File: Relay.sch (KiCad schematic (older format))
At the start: 11 parts, among them K1 1461069-5, Q1 2N3404, U1 LTV-816S

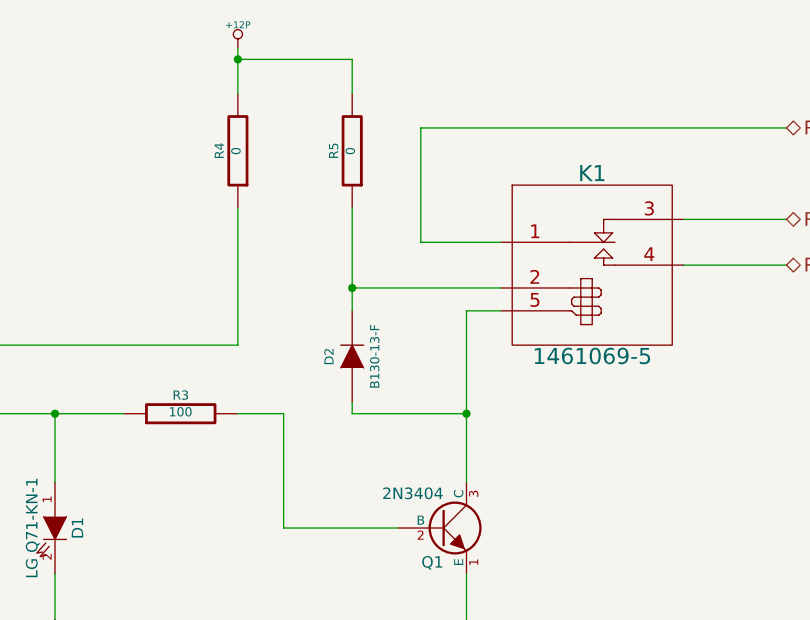
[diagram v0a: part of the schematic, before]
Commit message: Test points added, silk screen updates
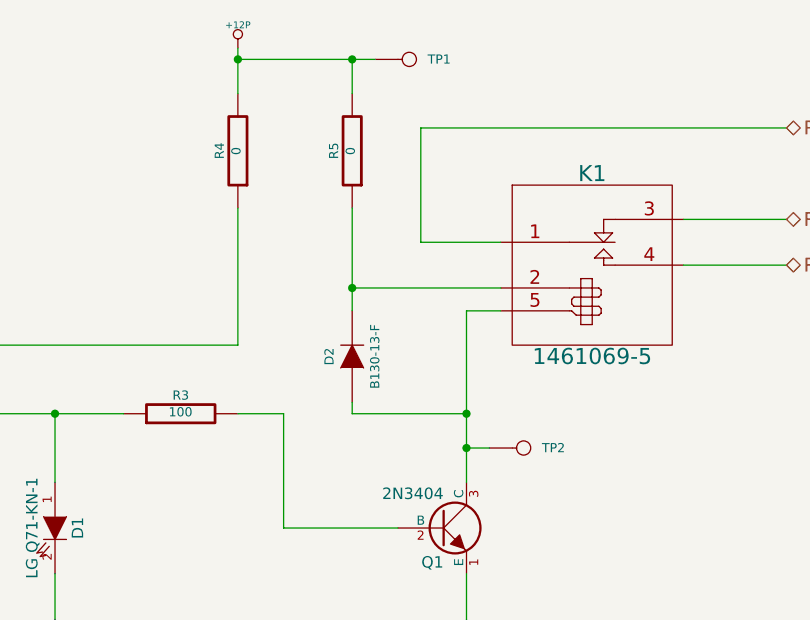
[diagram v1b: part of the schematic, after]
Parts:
- added TP1: +12P, symbol CONN_1
- added TP2: RLY_LOW, symbol CONN_1
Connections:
- net +12P: now also TP1.1
- net at D2.1 (A), K1.5 (COIL-), Q1.3 (C): now also TP2.1
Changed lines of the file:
@@
 	6100 3100 5900 3100
 $Comp
-L +12P #PWR1
+L +12P #PWR01
 U 1 1 52F17C6A
 P 5900 1500
-F 0 "#PWR1" H 5900 1470 30  0001 C CNN
+F 0 "#PWR01" H 5900 1470 30  0001 C CNN
 F 1 "+12P" H 5900 1600 30  0000 C CNN
 F 2 "" H 5900 1500 60  0000 C CNN
@@
 	6400 1700 6400 1550
 Wire Wire Line
-	6400 1550 5900 1550
+	5900 1550 6500 1550
 Connection ~ 5900 1550
 Wire Wire Line
@@
 Connection ~ 6400 2550
 $Comp
-L GND_RELAY #PWR2
+L GND_RELAY #PWR02
 U 1 1 53152624
 P 6900 4800
-F 0 "#PWR2" H 6900 4800 30  0001 C CNN
+F 0 "#PWR02" H 6900 4800 30  0001 C CNN
 F 1 "GND_RELAY" H 6900 4730 30  0000 C CNN
 F 2 "" H 6900 4800 60  0000 C CNN
@@
 	1    0    0    -1
 $EndComp
+$Comp
+L CONN_1 TP2
+U 1 1 532249E8
+P 7150 3250
+F 0 "TP2" H 7230 3250 40  0000 L CNN
+F 1 "RLY_LOW" H 7150 3305 30  0001 C CNN
+F 2 "" H 7150 3250 60  0000 C CNN
+F 3 "" H 7150 3250 60  0000 C CNN
+	1    7150 3250
+	1    0    0    -1
+$EndComp
+Wire Wire Line
+	7000 3250 6900 3250
+Connection ~ 6900 3250
+$Comp
+L CONN_1 TP1
+U 1 1 53224A4C
+P 6650 1550
+F 0 "TP1" H 6730 1550 40  0000 L CNN
+F 1 "+12P" H 6650 1605 30  0001 C CNN
+F 2 "" H 6650 1550 60  0000 C CNN
+F 3 "" H 6650 1550 60  0000 C CNN
+	1    6650 1550
+	1    0    0    -1
+$EndComp
+Connection ~ 6400 1550
 $EndSCHEMATC

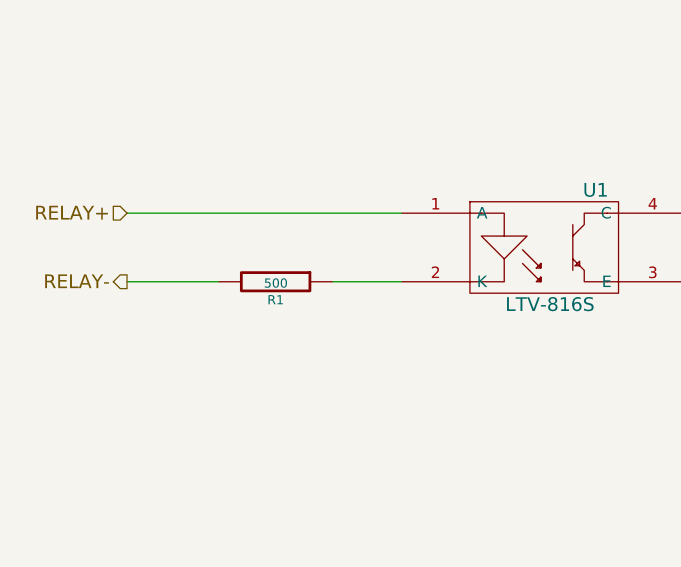
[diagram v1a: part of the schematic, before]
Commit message: Assigned values to passives in Arduino, power adjustment monitor, relay and terminal block schematics
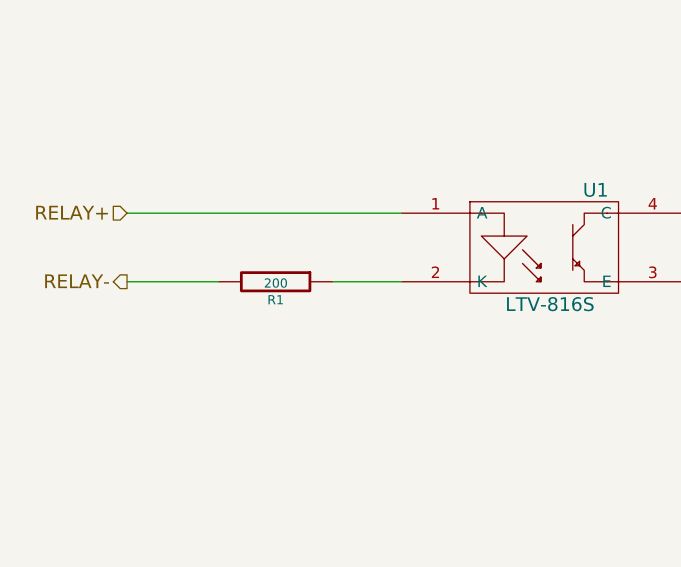
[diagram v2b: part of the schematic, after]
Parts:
- R1: value 500 -> 200
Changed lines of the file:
@@
 P 2650 3100
 F 0 "R1" V 2730 3100 40  0000 C CNN
-F 1 "500" V 2657 3101 40  0000 C CNN
+F 1 "200" V 2657 3101 40  0000 C CNN
 F 2 "" V 2580 3100 30  0000 C CNN
 F 3 "" H 2650 3100 30  0000 C CNN

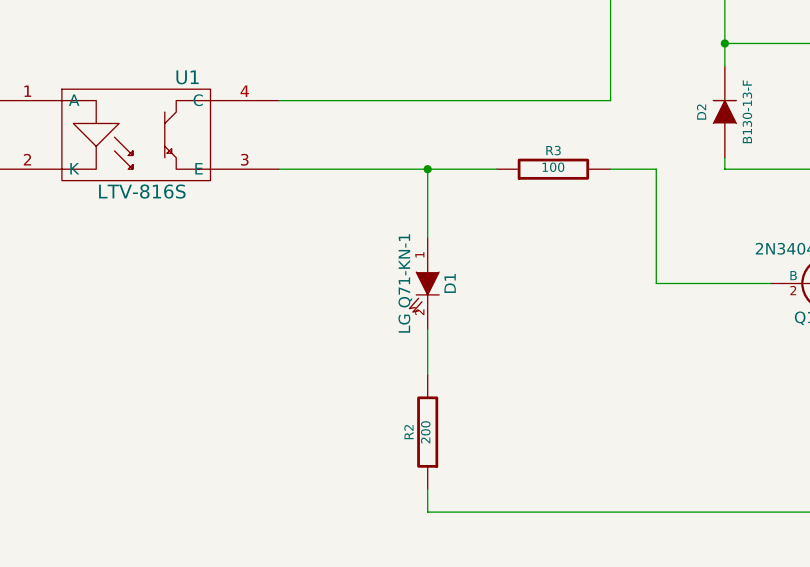
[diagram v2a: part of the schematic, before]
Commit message: Back-annotated footprints into the schematic
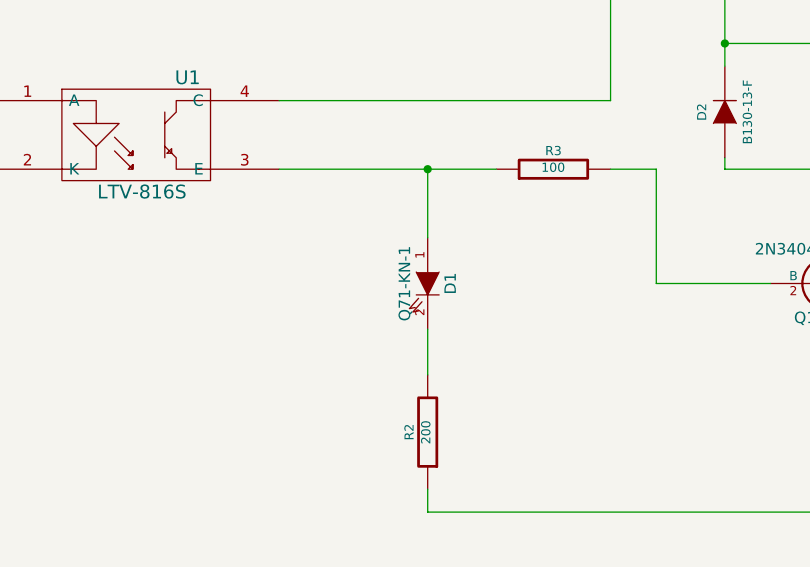
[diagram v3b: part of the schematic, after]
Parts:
- D1: value LG Q71-KN-1 -> Q71-KN-1; footprint (none) -> LEDs:LED-0603
- D2: footprint (none) -> Diodes_SMD:Diode-SMA_Standard
- K1: footprint (none) -> BenchBudEE:TE-SPDT
- Q1: footprint (none) -> SMD_Packages:SOT23EBC
- R1, R2, R3, R4, R5, R6: footprint (none) -> SMD_Packages:SM0805
- TP1, TP2: footprint (none) -> BenchBudEE:TestPointTH
- U1: footprint (none) -> BenchBudEE:4-SMD
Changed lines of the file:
@@
 F 0 "R3" V 5730 3100 40  0000 C CNN
 F 1 "100" V 5657 3101 40  0000 C CNN
-F 2 "" V 5580 3100 30  0000 C CNN
+F 2 "SMD_Packages:SM0805" V 5580 3100 30  0001 C CNN
 F 3 "" H 5650 3100 30  0000 C CNN
 	1    5650 3100
@@
 F 0 "Q1" H 6800 3450 50  0000 R CNN
 F 1 "2N3404" H 6800 3750 50  0000 R CNN
-F 2 "" H 6800 3600 60  0000 C CNN
+F 2 "SMD_Packages:SOT23EBC" H 6800 3600 60  0001 C CNN
 F 3 "" H 6800 3600 60  0000 C CNN
 F 4 "Diodes Inc" H 6800 3600 60  0001 C CNN "MFG Name"
@@
 P 5100 3600
 F 0 "D1" H 5100 3700 50  0000 C CNN
-F 1 "LG Q71-KN-1" H 5100 3500 50  0000 C CNN
-F 2 "" H 5100 3600 60  0000 C CNN
+F 1 "Q71-KN-1" H 5100 3500 50  0000 C CNN
+F 2 "LEDs:LED-0603" H 5100 3600 60  0001 C CNN
 F 3 "" H 5100 3600 60  0000 C CNN
 	1    5100 3600
@@
 F 0 "K1" H 7450 2550 70  0000 C CNN
 F 1 "1461069-5" H 7450 1750 70  0000 C CNN
-F 2 "" H 7450 2300 60  0000 C CNN
+F 2 "BenchBudEE:TE-SPDT" H 7450 2300 60  0001 C CNN
 F 3 "" H 7450 2300 60  0000 C CNN
 	1    7450 2300
@@
 F 0 "R6" V 6980 4250 40  0000 C CNN
 F 1 "0" V 6907 4251 40  0000 C CNN
-F 2 "" V 6830 4250 30  0000 C CNN
+F 2 "SMD_Packages:SM0805" V 6830 4250 30  0001 C CNN
 F 3 "" H 6900 4250 30  0000 C CNN
 	1    6900 4250
@@
 F 0 "R2" V 5180 4250 40  0000 C CNN
 F 1 "200" V 5107 4251 40  0000 C CNN
-F 2 "" V 5030 4250 30  0000 C CNN
+F 2 "SMD_Packages:SM0805" V 5030 4250 30  0001 C CNN
 F 3 "" H 5100 4250 30  0000 C CNN
 	1    5100 4250
@@
 F 0 "R4" V 5980 1950 40  0000 C CNN
 F 1 "0" V 5907 1951 40  0000 C CNN
-F 2 "" V 5830 1950 30  0000 C CNN
+F 2 "SMD_Packages:SM0805" V 5830 1950 30  0001 C CNN
 F 3 "" H 5900 1950 30  0000 C CNN
 	1    5900 1950
@@
 F 0 "R1" V 2730 3100 40  0000 C CNN
 F 1 "200" V 2657 3101 40  0000 C CNN
-F 2 "" V 2580 3100 30  0000 C CNN
+F 2 "SMD_Packages:SM0805" V 2580 3100 30  0001 C CNN
 F 3 "" H 2650 3100 30  0000 C CNN
 	1    2650 3100
@@
 F 0 "D2" H 6400 2950 40  0000 C CNN
 F 1 "B130-13-F" H 6400 2750 40  0000 C CNN
-F 2 "" H 6400 2850 60  0000 C CNN
+F 2 "Diodes_SMD:Diode-SMA_Standard" H 6400 2850 60  0001 C CNN
 F 3 "" H 6400 2850 60  0000 C CNN
 	1    6400 2850
@@
 F 0 "U1" H 4050 3200 60  0000 C CNN
 F 1 "LTV-816S" H 3850 2700 60  0000 C CNN
-F 2 "" H 3850 2950 60  0000 C CNN
+F 2 "BenchBudEE:4-SMD" H 3850 2950 60  0001 C CNN
 F 3 "" H 3850 2950 60  0000 C CNN
 F 4 "LTV-816S" H 3850 2950 60  0001 C CNN "MFG Part Number"
@@
 F 0 "R5" V 6480 1950 40  0000 C CNN
 F 1 "0" V 6407 1951 40  0000 C CNN
-F 2 "" V 6330 1950 30  0000 C CNN
+F 2 "SMD_Packages:SM0805" V 6330 1950 30  0001 C CNN
 F 3 "" H 6400 1950 30  0000 C CNN
 	1    6400 1950
@@
 F 0 "TP2" H 7230 3250 40  0000 L CNN
 F 1 "RLY_LOW" H 7150 3305 30  0001 C CNN
-F 2 "" H 7150 3250 60  0000 C CNN
+F 2 "BenchBudEE:TestPointTH" H 7150 3250 60  0001 C CNN
 F 3 "" H 7150 3250 60  0000 C CNN
 	1    7150 3250
@@
 F 0 "TP1" H 6730 1550 40  0000 L CNN
 F 1 "+12P" H 6650 1605 30  0001 C CNN
-F 2 "" H 6650 1550 60  0000 C CNN
+F 2 "BenchBudEE:TestPointTH" H 6650 1550 60  0001 C CNN
 F 3 "" H 6650 1550 60  0000 C CNN
 	1    6650 1550

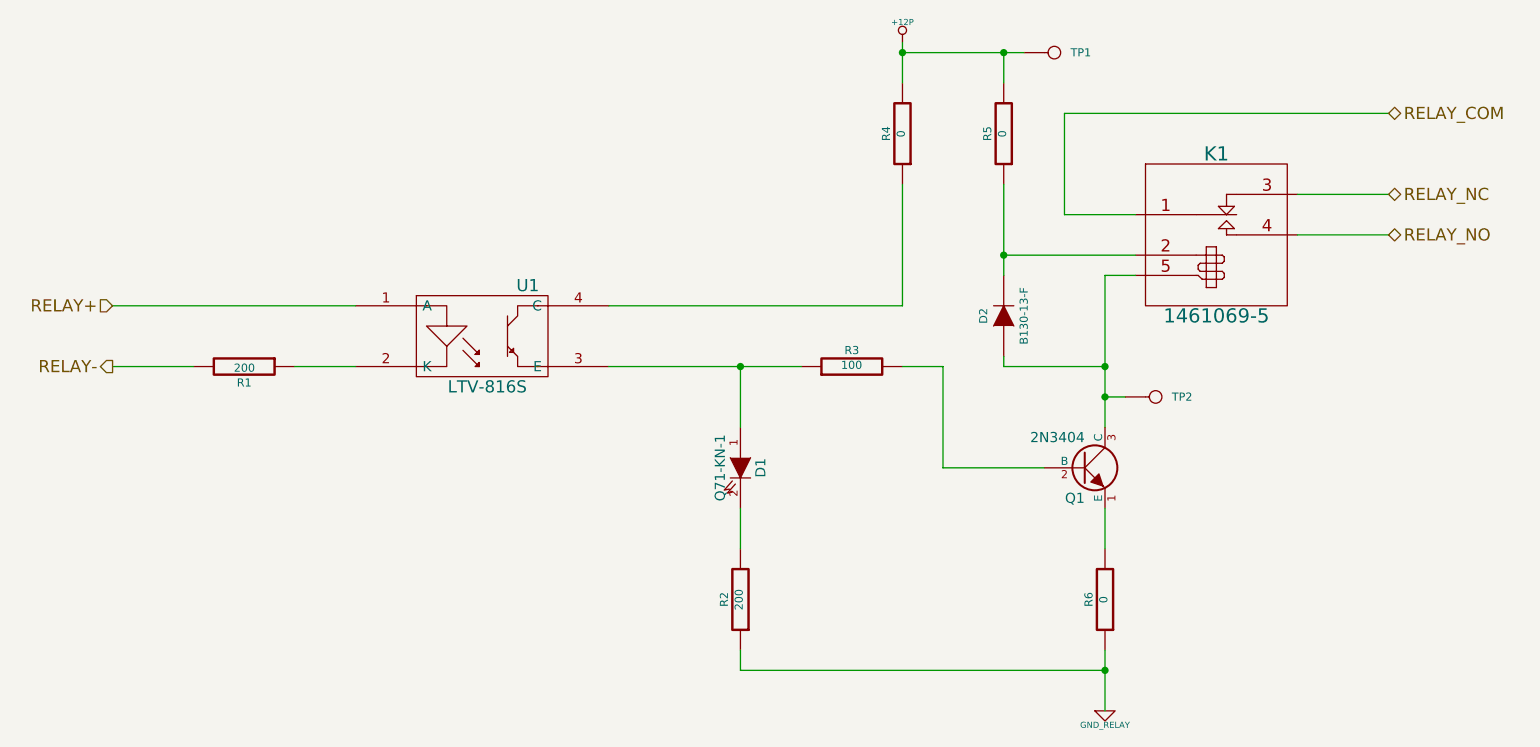
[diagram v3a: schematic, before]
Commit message: Final part numbers added to schematic, cross-checked KiCAD BOM against manual BOM
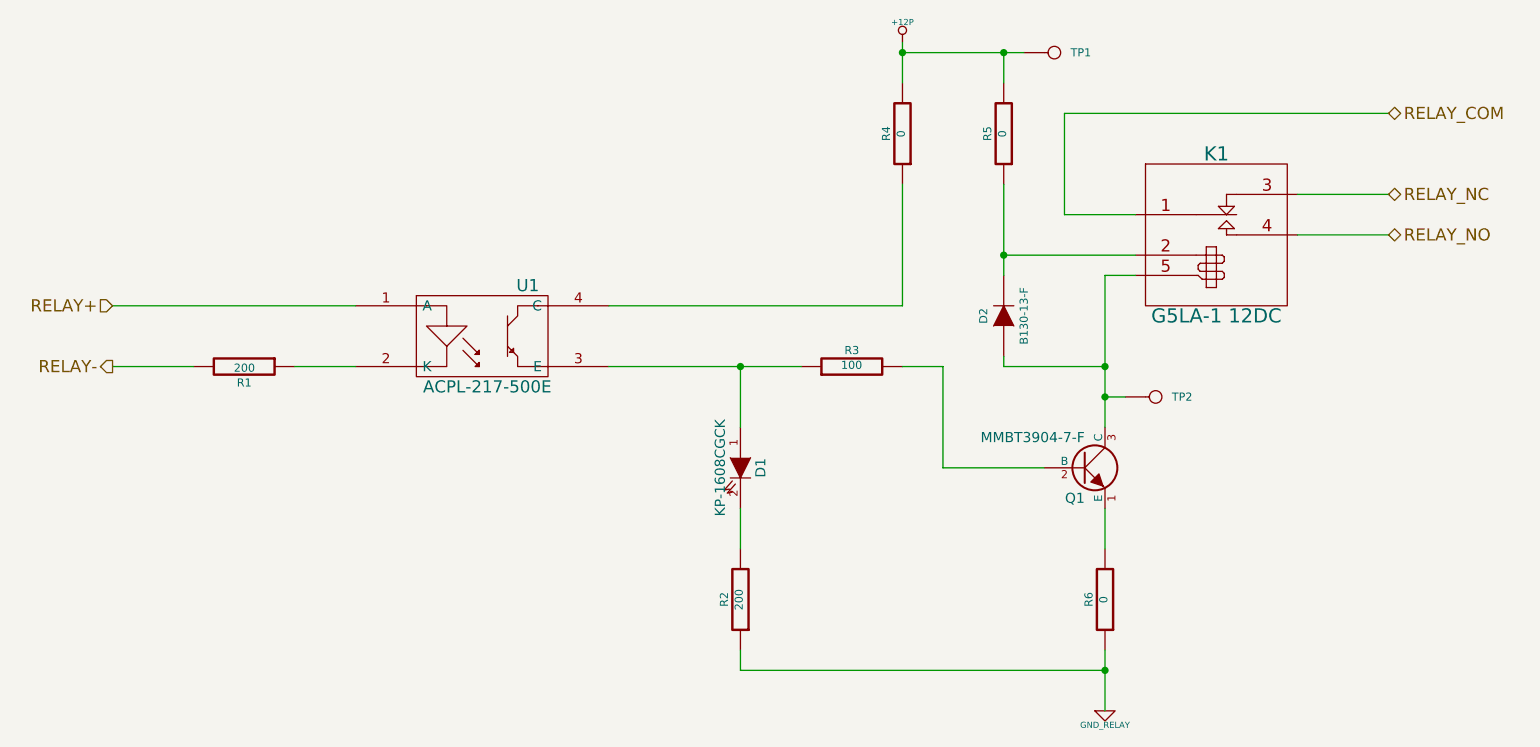
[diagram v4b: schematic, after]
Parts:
- D1: value Q71-KN-1 -> KP-1608CGCK
- K1: value 1461069-5 -> G5LA-1 12DC
- Q1: value 2N3404 -> MMBT3904-7-F
- U1: value LTV-816S -> ACPL-217-500E
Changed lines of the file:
@@
 P 6800 3600
 F 0 "Q1" H 6800 3450 50  0000 R CNN
-F 1 "2N3404" H 6800 3750 50  0000 R CNN
+F 1 "MMBT3904-7-F" H 6800 3750 50  0000 R CNN
 F 2 "SMD_Packages:SOT23EBC" H 6800 3600 60  0001 C CNN
 F 3 "" H 6800 3600 60  0000 C CNN
@@
 P 5100 3600
 F 0 "D1" H 5100 3700 50  0000 C CNN
-F 1 "Q71-KN-1" H 5100 3500 50  0000 C CNN
+F 1 "KP-1608CGCK" H 5100 3500 50  0000 C CNN
 F 2 "LEDs:LED-0603" H 5100 3600 60  0001 C CNN
 F 3 "" H 5100 3600 60  0000 C CNN
@@
 P 7450 2300
 F 0 "K1" H 7450 2550 70  0000 C CNN
-F 1 "1461069-5" H 7450 1750 70  0000 C CNN
+F 1 "G5LA-1 12DC" H 7450 1750 70  0000 C CNN
 F 2 "BenchBudEE:TE-SPDT" H 7450 2300 60  0001 C CNN
 F 3 "" H 7450 2300 60  0000 C CNN
@@
 P 3850 2950
 F 0 "U1" H 4050 3200 60  0000 C CNN
-F 1 "LTV-816S" H 3850 2700 60  0000 C CNN
+F 1 "ACPL-217-500E" H 3850 2700 60  0000 C CNN
 F 2 "BenchBudEE:4-SMD" H 3850 2950 60  0001 C CNN
 F 3 "" H 3850 2950 60  0000 C CNN
